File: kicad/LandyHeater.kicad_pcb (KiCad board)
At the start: 4 copper layers, 80 x 50 mm, 139 parts, among them J1 12V IN, J2 AUTOTERM, J3 1-Wire, J4 Taster/LED, J5 USB4105-GF-A-060, Q1 2N7002K, SW1 RESET, SW2 BOOT, SW3 DIAG, U1 TPD2EUSB30DRTR, U2 TPS259470LRPWR, U3 LMR43620MSC3RPERQ1, U4 ESP32-S3-WROOM-1U-N16R8, U5 TPS3808G33DBVR, U6 RV-8263-C8, U7 TXU0202QDCURQ1, U8 TPS22945DCKR, U9 BCR421UW6Q-7

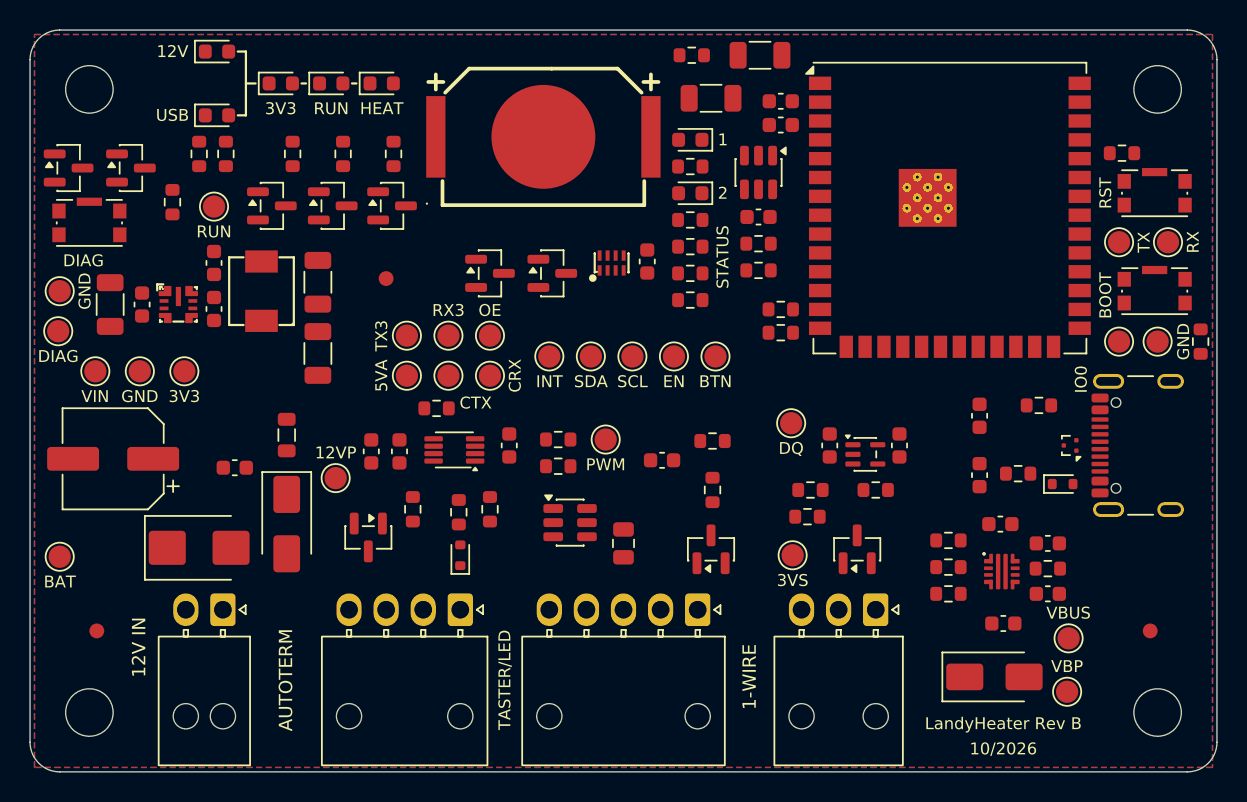
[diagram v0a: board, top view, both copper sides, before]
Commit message: Route critical paths by hand: 12 V input, buck, USB-C, eFuse (step 6.3)
- tools/route_manual.py: reproducible manual routes, vias and R:-zones for
  blocks A-D with datasheet references; project DRC 0 violations
- USB placement refinements found while routing (U1, D3/R1/R2, C17/C18,
  R6/C4), checker keepout for the pair at U1
- USB pair routed 0.25/0.15 mm: net class clearance 0.15 overrides the
  0.13 DRU rule; not loosened (~92 ohm, fine for USB FS)
- silkscreen.py / route_manual.py: avoid SWIG crashes after BOARD.Remove()
- zones.py: routing-phase fill only unfills the outer GND pours
- Routing_Bericht.md with render

Co-Authored-By: Claude Opus 5.5 <noreply@anthropic.com>
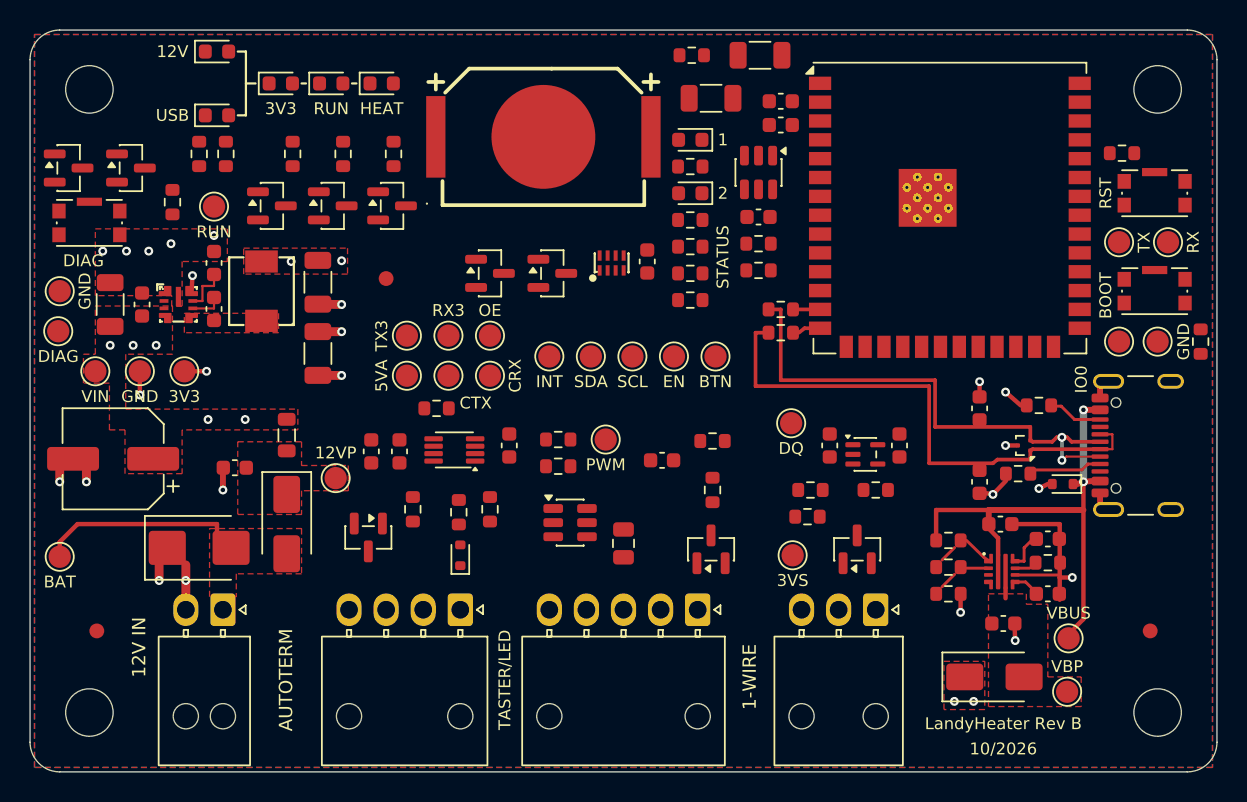
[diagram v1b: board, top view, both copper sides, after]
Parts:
- moved U1 3.10 mm to (167.0, 128.0)
- moved C17 0.50 mm to (164.0, 125.5), turned to 90 degrees
- moved C18 0.45 mm to (164.0, 130.4), turned to -90 degrees
- moved R6 0.40 mm to (168.6, 135.9)
- moved C4 0.30 mm to (168.6, 134.3)
- turned D3 to 180 degrees
- turned R1 to 180 degrees
- turned R2 to 180 degrees
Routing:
- net USB_DP_C: track 0.00 -> 35.2 mm
- net USB_DN_C: track 0.00 -> 33.9 mm, vias 0 -> 2
- net /Versorgung/USB_VBUS: track 0.00 -> 30.6 mm, vias 0 -> 2
- net GND: track 0.00 -> 30.2 mm, vias 0 -> 21
- net /Versorgung/BATT_12V_IN: track 0.00 -> 12.7 mm
- net 3V3_CORE: track 0.00 -> 4.14 mm, vias 0 -> 5
- net /Versorgung/CC1: track 0.00 -> 3.89 mm
- net Net-(U2-EN/UVLO): track 0.00 -> 3.20 mm
- net /Versorgung/CC2: track 0.00 -> 2.69 mm
- net Net-(U3-VCC): track 0.00 -> 2.60 mm
- net Net-(U2-OVLO): track 0.00 -> 2.58 mm
- net Net-(U2-ITIMER): track 0.00 -> 1.91 mm
- net Net-(U3-BOOT): track 0.00 -> 1.55 mm
- net Net-(U2-DVDT): track 0.00 -> 0.97 mm
- net Net-(U4-USB_D+): track 0.00 -> 0.78 mm
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- added copper zone on F.Cu, net /Versorgung/BATT_12V_IN
- added copper zone on F.Cu, net /Versorgung/SW_BUCK
- added copper zone on F.Cu, net 12V_PROT
- added copper zone on F.Cu, net 3V3_CORE
- added copper zone on F.Cu, net VBUS_PROT
- added copper zone on F.Cu, net VIN_SYS

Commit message: Hand-route the module escape and connect all plane pads (steps 6.3/6.4)
- route_manual.py blocks E-G: fine-pitch inner pins (U7, U8), left module
  pin row (EN, status LEDs, DIAG, I2C pull-ups, fan-out vias), exits for
  the 12V_PROT/VBUS_PROT diagnostic feeds
- swap R33/R34 so each status-LED net has adjacent pads (no interleave)
- route_planevias.py: plane vias for every GND/3V3/VIN pad, respects the
  L3 split, module body and coin cell; all plane pads connected
- freeroute.py: reproducible Freerouting step (locked hand routes, R:
  zones as keepouts, L3 as power layer, via cost 8, best of N runs,
  hard timeout, analytics off); result not yet applied
- project DRC: 0 errors

Co-Authored-By: Claude Opus 5.5 <noreply@anthropic.com>
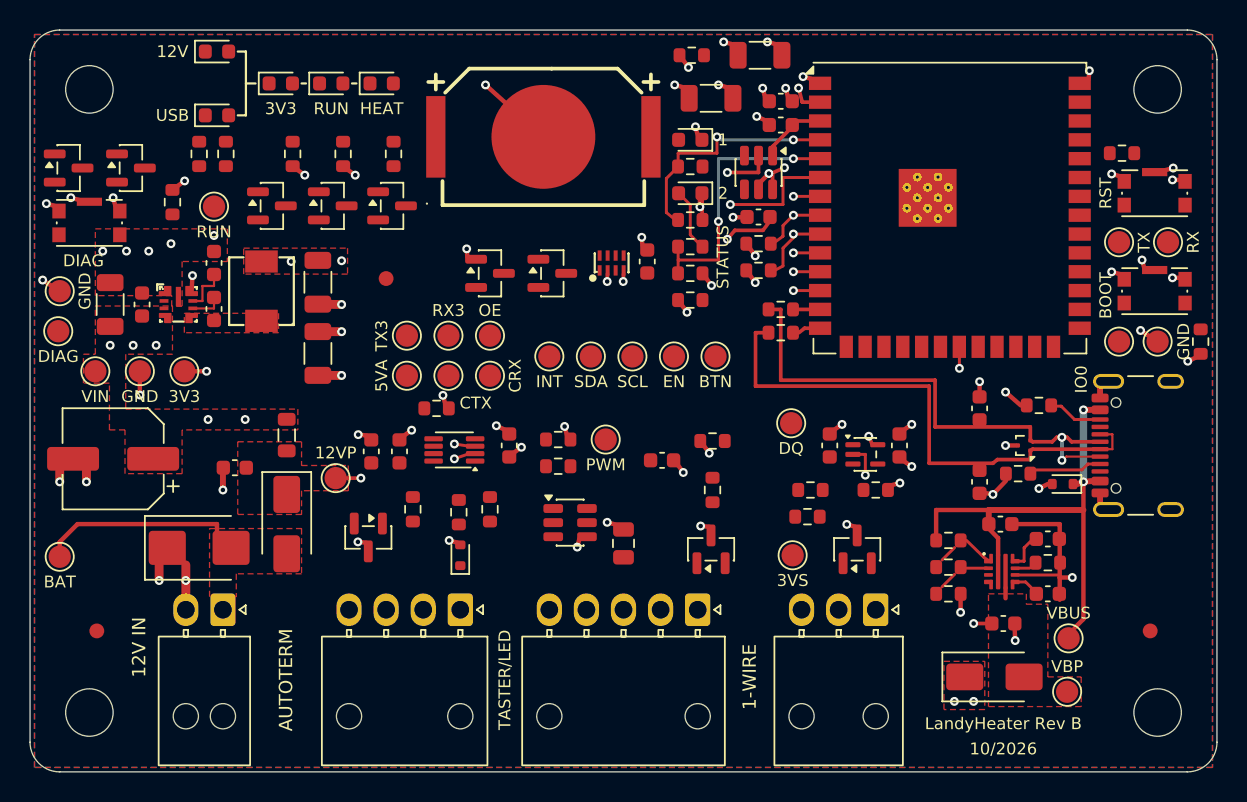
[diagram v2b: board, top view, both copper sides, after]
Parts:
- moved R33 1.80 mm to (144.5, 114.6)
- moved R34 1.80 mm to (144.5, 112.8)
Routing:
- net GND: track 30.2 -> 69.5 mm, vias 21 -> 64
- net STATUS_LED_2: track 0.00 -> 17.2 mm, vias 0 -> 2
- net 3V3_CORE: track 4.14 -> 19.7 mm, vias 5 -> 25
- net STATUS_LED_1: track 0.00 -> 14.9 mm, vias 0 -> 2
- net DIAG_RUN: track 0.00 -> 7.52 mm, vias 0 -> 1
- net /ESP32 und RTC/I2C_SCL: track 0.00 -> 4.52 mm, vias 0 -> 1
- net Net-(D21-A): track 0.00 -> 3.97 mm
- net /ESP32 und RTC/I2C_SDA: track 0.00 -> 3.84 mm, vias 0 -> 1
- net /ESP32 und RTC/EN: track 0.00 -> 3.13 mm
- net 12V_PROT: track 0.00 -> 1.70 mm, vias 0 -> 1
- net AUTOTERM_TX_3V3: track 0.00 -> 1.45 mm, vias 0 -> 1
- net AUTOTERM_RX_3V3: track 0.00 -> 1.45 mm, vias 0 -> 1
- net AUTOTERM_OE: track 0.00 -> 1.45 mm, vias 0 -> 1
- net /ESP32 und RTC/RTC_INT_N: track 0.00 -> 1.45 mm, vias 0 -> 1
- net VBUS_PROT: track 0.70 -> 1.92 mm, vias 0 -> 1
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
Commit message: Hand-route long L4 trunks: DIAG_RUN and diagnostic feeds (block H)
LED2 landing moved above the DIAG lane; project DRC 0 errors.

Co-Authored-By: Claude Opus 5.5 <noreply@anthropic.com>
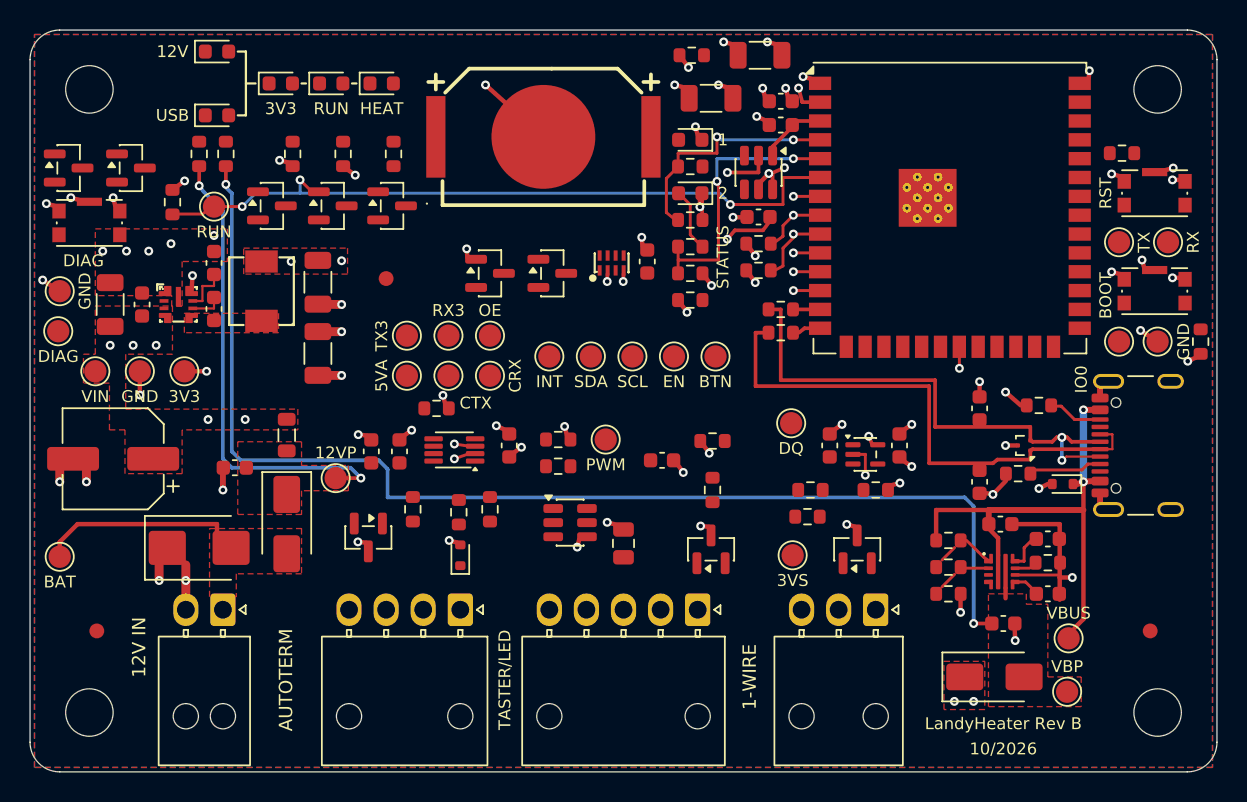
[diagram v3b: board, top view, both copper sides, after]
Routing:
- net VBUS_PROT: track 1.92 -> 81.6 mm, vias 1 -> 2
- net DIAG_RUN: track 7.52 -> 47.8 mm, vias 1 -> 3
- net 12V_PROT: track 1.70 -> 31.7 mm, vias 1 -> 2

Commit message: Add Freerouting baseline for slow signals (best run, 23 connections left)
Co-Authored-By: Claude Opus 5.5 <noreply@anthropic.com>
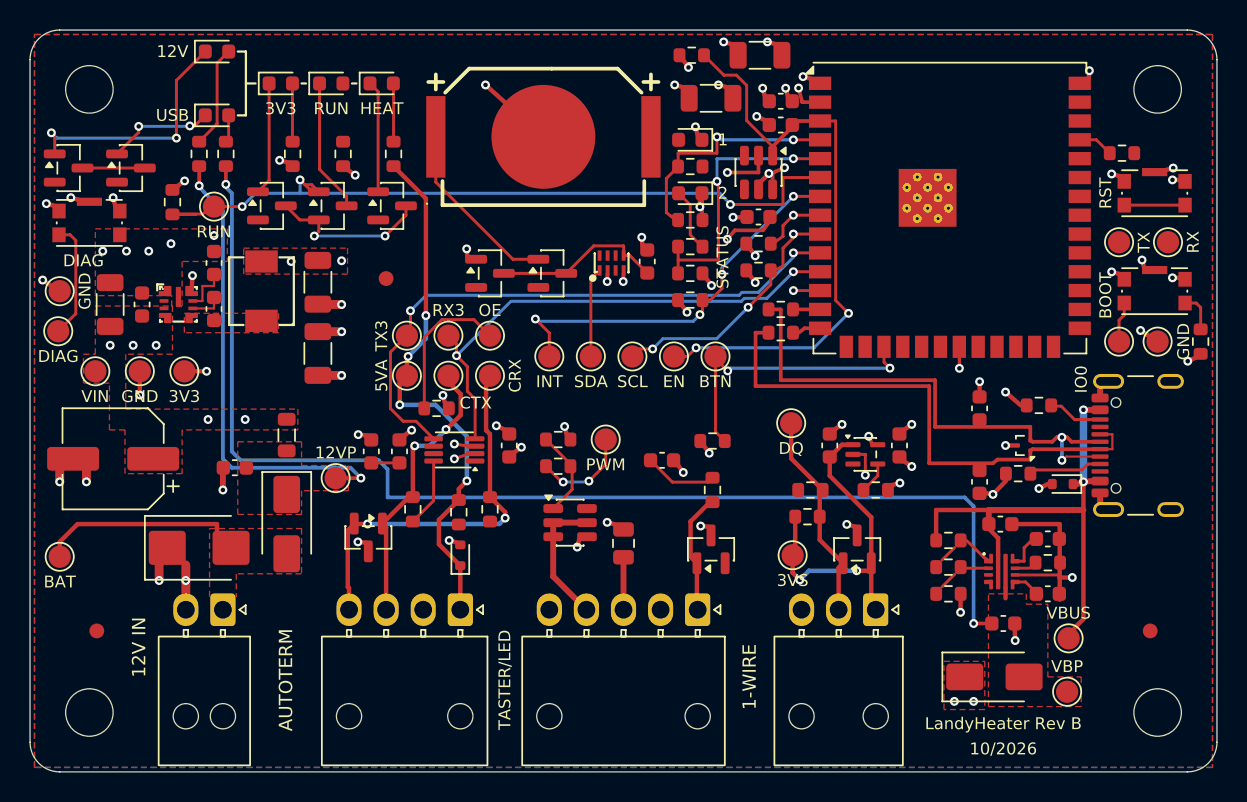
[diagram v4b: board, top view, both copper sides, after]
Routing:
- net /ESP32 und RTC/EN: track 3.13 -> 44.5 mm, vias 0 -> 2
- net AUTOTERM_TX_3V3: track 1.45 -> 40.3 mm, vias 1 -> 2
- net AUTOTERM_5V: track 0.00 -> 36.2 mm, vias 0 -> 4
- net AUTOTERM_RX_3V3: track 1.45 -> 34.5 mm, vias 1 -> 2
- net /ESP32 und RTC/RTC_INT_N: track 1.45 -> 28.3 mm, vias 1 -> 4
- net /AUTOTERM und 1-Wire/CTRL_RX: track 0.00 -> 26.6 mm, vias 0 -> 2
- net BUTTON_N: track 0.00 -> 24.8 mm, vias 0 -> 2
- net /Taster und Anzeige/DIAG_K: track 0.00 -> 23.3 mm, vias 0 -> 2
- net /AUTOTERM und 1-Wire/3V3_SENSOR_SW: track 0.00 -> 23.1 mm, vias 0 -> 2
- net /AUTOTERM und 1-Wire/CTRL_TX: track 0.00 -> 19.1 mm, vias 0 -> 2
- net Net-(D11-K): track 0.00 -> 16.7 mm, vias 0 -> 2
- net /AUTOTERM und 1-Wire/1WIRE_DQ_C: track 0.00 -> 14.3 mm
- net /ESP32 und RTC/I2C_SCL: track 4.52 -> 17.4 mm, vias 1 -> 3
- net /ESP32 und RTC/VBAT: track 0.00 -> 12.1 mm
- net /ESP32 und RTC/RTC_VDD: track 0.00 -> 11.6 mm
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
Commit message: Close all remaining connections (route_finish + maze router)
- route_finish.py: hand fixes after Freerouting (buttons/UART test points,
  EN under the module, diag LEDs, DIAG_K, VBAT, U7 area) plus a generated
  section from maze_route.py
- maze_route.py: deterministic A* two-layer router for the leftovers,
  emits explicit T()/V() lines; no via-in-pad, project clearances
- route_manual: LED1 enters R32 from the left, U6 GND vias spread for
  RTC_INT, SCL stays on L1, GND Buck corner trimmed
- project DRC: 0 violations, 0 unconnected

Co-Authored-By: Claude Opus 5.5 <noreply@anthropic.com>
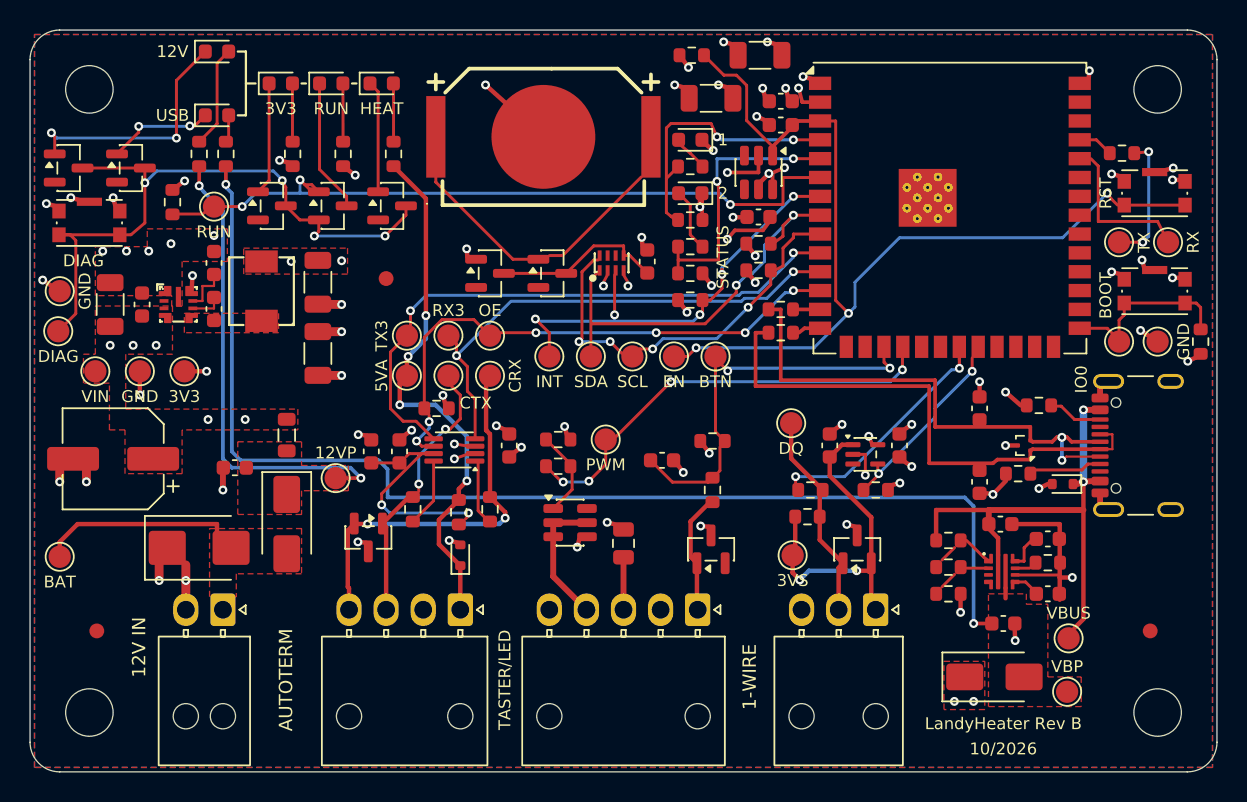
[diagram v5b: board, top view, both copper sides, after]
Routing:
- net AUTOTERM_OE: track 12.0 -> 35.4 mm, vias 1 -> 6
- net /ESP32 und RTC/EN: track 44.5 -> 67.4 mm, vias 2 -> 3
- net BUTTON_LED_PWM: track 6.63 -> 28.6 mm, vias 2 -> 4
- net /Taster und Anzeige/DIAG_K: track 23.3 -> 44.6 mm, vias 2 -> 4
- net /ESP32 und RTC/I2C_SDA: track 10.6 -> 27.8 mm, vias 1 -> 2
- net 1WIRE_DQ: track 3.09 -> 17.4 mm, vias 1 -> 2
- net /AUTOTERM und 1-Wire/AUTOTERM_5V_F: track 1.90 -> 14.6 mm, vias 0 -> 2
- net SENSOR_EN: track 2.15 -> 12.6 mm, vias 0 -> 2
- net /ESP32 und RTC/I2C_SCL: track 17.4 -> 26.9 mm, vias 3 -> 4
- net Net-(U4-RXD0): track 0.00 -> 9.33 mm
- net /ESP32 und RTC/VBAT: track 12.1 -> 20.5 mm
- net Net-(R11-Pad2): track 0.00 -> 8.24 mm, vias 0 -> 2
- net /ESP32 und RTC/BOOT_N: track 5.40 -> 12.2 mm
- net Net-(D19-A): track 0.00 -> 3.93 mm
- net Net-(U7-B2): track 0.00 -> 3.77 mm
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
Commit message: Fill outer GND pours, add GND stitching, routing checks (step 6.7)
- EN no longer runs under the module body (via removed, L4 path along
  the module top edge); DIAG_K stub tidied
- stitch_gnd.py: 148 GND vias where both outer fills cover the via
- zones.py: solid connection for five GND pads inside hand-made GND
  areas (starved thermal otherwise)
- check_routing.py: Y-03 split crossing, vias under coin cell/module,
  acute angles, statistics
- DRC report output/DRC_Routing.rpt: 0 violations, 0 unconnected

Co-Authored-By: Claude Opus 5.5 <noreply@anthropic.com>
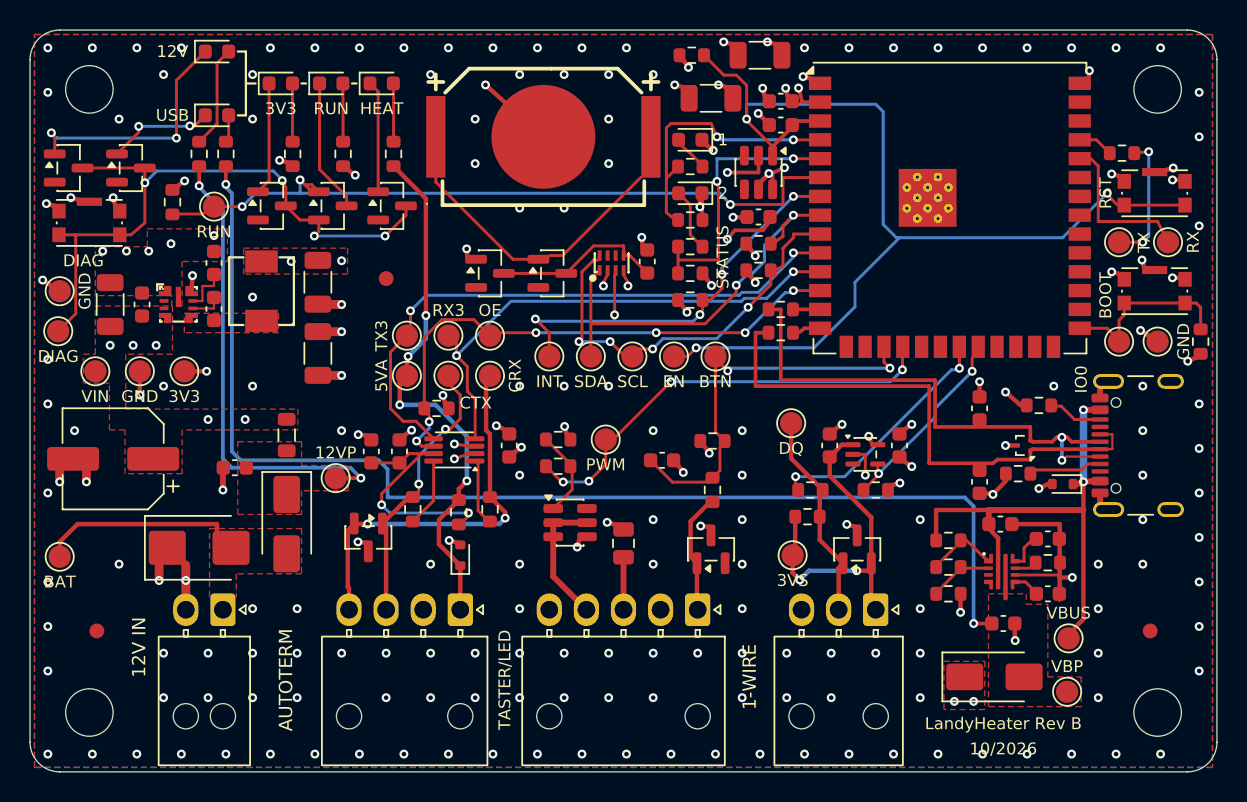
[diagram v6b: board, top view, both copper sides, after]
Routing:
- net /ESP32 und RTC/EN: track 67.4 -> 72.5 mm
- net /Taster und Anzeige/DIAG_K: track 44.6 -> 43.7 mm
- net GND: track 70.1 -> 70.2 mm, vias 64 -> 212

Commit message: Rework USB pair: 90 ohm per JLCPCB calculator, coupled, arcs, length-matched
- JLCPCB impedance calculator (JLC04161H-7628, L1/L2): 0.247 mm plain,
  0.235 mm coplanar at 0.15 mm gap -> 0.24/0.15 mm; USB net class and
  DRU rule updated
- pair stays coupled from U1 to the series resistors; C17/C18 (DNP)
  staggered on the outside, signal pad on the line
- all bends as concentric arcs (new arc helper in route_manual.py)
- D+ meander: D- 29.358 mm, D+ 29.357 mm
- DRC 0 violations / 0 unconnected; report and close-up updated

Co-Authored-By: Claude Opus 5.5 <noreply@anthropic.com>
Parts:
- moved C17 1.98 mm to (162.3, 126.6)
- moved C18 1.04 mm to (164.1, 129.4)
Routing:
- net USB_DP_C: track 35.2 -> 31.4 mm
- net GND: track 70.2 -> 71.3 mm
- net USB_DN_C: track 33.9 -> 32.8 mm
